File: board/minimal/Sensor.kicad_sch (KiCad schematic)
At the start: 27 parts, among them Q2 DMP6050SSD, U5 TLV73318PDBV, U6 PCA9306D, U7 ICM-20948, U8 BME280, U9 INA260

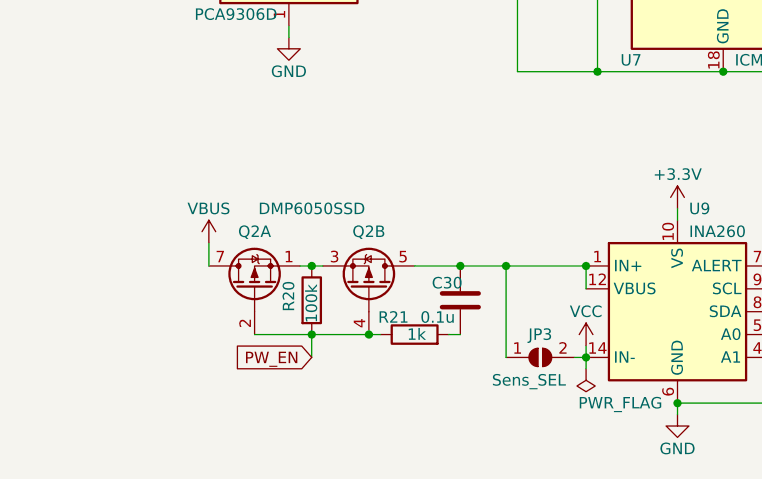
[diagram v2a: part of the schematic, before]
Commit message: add some connectors
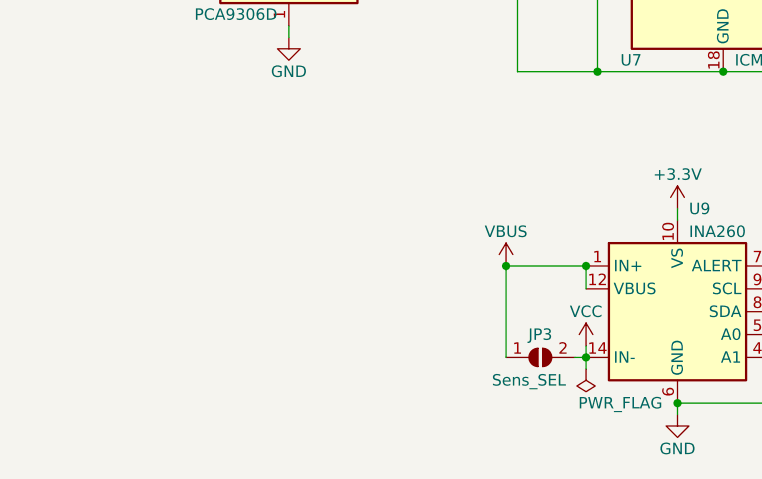
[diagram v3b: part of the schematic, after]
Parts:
- removed C30: 0.1u, Capacitor_SMD:C_0201_0603Metric, symbol Device:C
- removed Q2: DMP6050SSD, Package_SO:SOIC-8_3.9x4.9mm_P1.27mm, symbol Transistor_FET:DMP6050SSD
- removed R20: 100k, Resistor_SMD:R_0603_1608Metric, symbol Device:R
- removed R21: 1k, Resistor_SMD:R_0603_1608Metric, symbol Device:R
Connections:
- net VBUS: now also JP3.1 (A), U9.1 (IN+), U9.12 (VBUS), U9.2 (IN+), U9.3 (IN+)

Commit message: change imu to BNO086
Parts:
- removed C23, C24: 1u, Capacitor_SMD:C_0201_0603Metric, symbol Device:C
- removed C25, C26, C27: 0.1u, Capacitor_SMD:C_0201_0603Metric, symbol Device:C
- removed JP1: I2C_Addr, Jumper:SolderJumper-2_P1.3mm_Open_RoundedPad1.0x1.5mm, symbol Jumper:SolderJumper_2_Open
- removed R13: 10k, Resistor_SMD:R_0603_1608Metric, symbol Device:R
- removed R14, R15, R16, R17: 1k, Resistor_SMD:R_0603_1608Metric, symbol Device:R
- removed R18: 200k, Resistor_SMD:R_0603_1608Metric, symbol Device:R
- removed U5: TLV73318PDBV, Package_TO_SOT_SMD:SOT-23-5, symbol Regulator_Linear:TLV73318PDBV
- removed U6: PCA9306D, Package_SON:X2SON-8_1.4x1mm_P0.35mm, symbol Interface:PCA9306D
- removed U7: ICM-20948, Sensor_Motion:InvenSense_QFN-24_3x3mm_P0.4mm, symbol Sensor_Motion:ICM-20948
- added C12, C21: 20p, Capacitor_SMD:C_0201_0603Metric, symbol Device:C
- added C22: 0.1u, Capacitor_SMD:C_0201_0603Metric, symbol Device:C
- added C45, C46: 100n, Capacitor_SMD:C_0201_0603Metric, symbol Device:C
- added R35, R36: 10k, Resistor_SMD:R_0603_1608Metric, symbol Device:R
- added TP6: BNO_{BOOT}, symbol Connector:TestPoint
- added U3: BNO086, BNO086, symbol BNO086:BNO086
- added Y1: ABS06-32.768KHZ-T, symbol Device:Crystal
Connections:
- net +1V8 is gone; now on net +3.3V: C28.1, C29.1
- net +3.3V: now also C45.1, C46.1, R35.1, R36.1, U3.28 (VDDIO), U3.3 (VDD)
- net GND: now also C12.1, C21.1, C22.1, C45.2, C46.2, U3.10 (CLKSEL0), U3.17 (SA0/H_MOSI), U3.2 (GND_1), U3.25 (GND_2), U3.5 (PS1), U3.6 (PS0/WAKE)
- net SCL: now also U3.19 (H_SCL/SCK/RX)
- net SDA: now also U3.20 (H_SDA/H_MISO/TX)
- new net: C21.2, U3.27 (XIN32), Y1.1
- new net: R36.2, U3.11 (NRST)
- new net: C12.2, U3.26 (XOUT32/CLKSEL1), Y1.2
- new net: R35.2, TP6.1, U3.4 (BOOTN)
- new net: C22.2, U3.9 (CAP)
- no-connect marks 4 -> 14
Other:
- moved on the sheet: C28, C29, C31, JP2, JP3, R19, U8, U9

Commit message: set footprint
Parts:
- TP1: renamed from TP6; footprint (none) -> TestPoint:TestPoint_Loop_D2.50mm_Drill1.85mm
- U7: renamed from U3; footprint BNO086 -> BNO086:BNO086
- Y2: renamed from Y1; footprint (none) -> ABRACON_Crystal:ABS06
- renumbered C45 to C28, C46 to C29, C22 to C30, C28 to C32, C29 to C33, C12 to C34, C21 to C35, JP3 to JP2, JP2 to JP3, R35 to R20, R36 to R21, R19 to R22, U9 to U6
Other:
- moved on the sheet: C31, JP2, U6

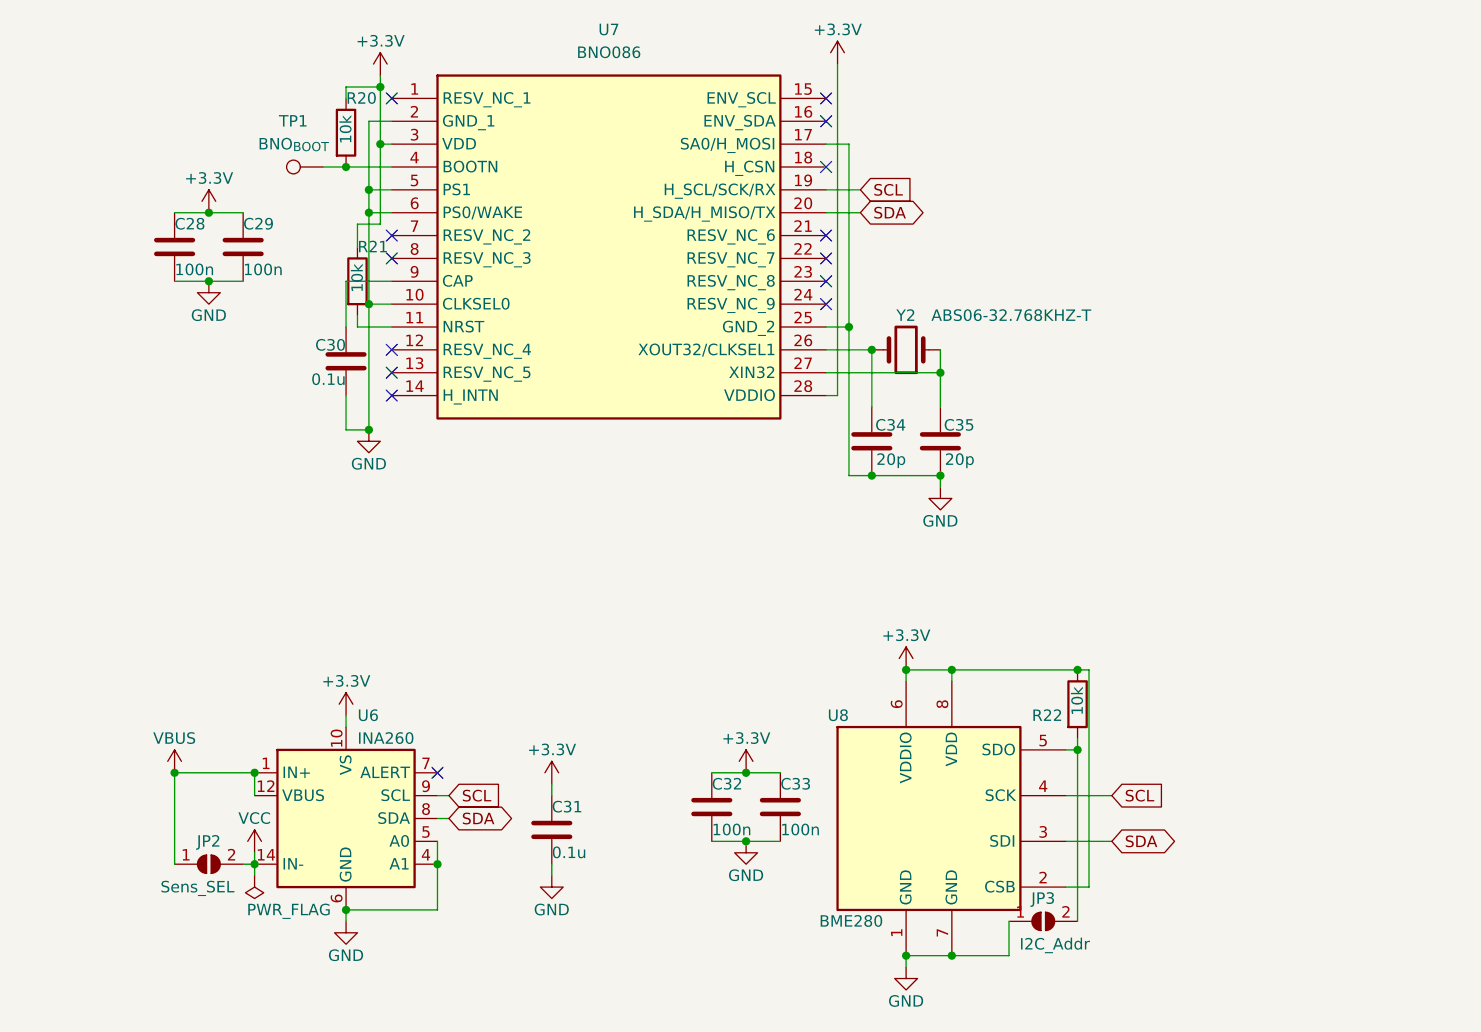
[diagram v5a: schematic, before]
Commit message: add testpoint for gnd and pic of schematics
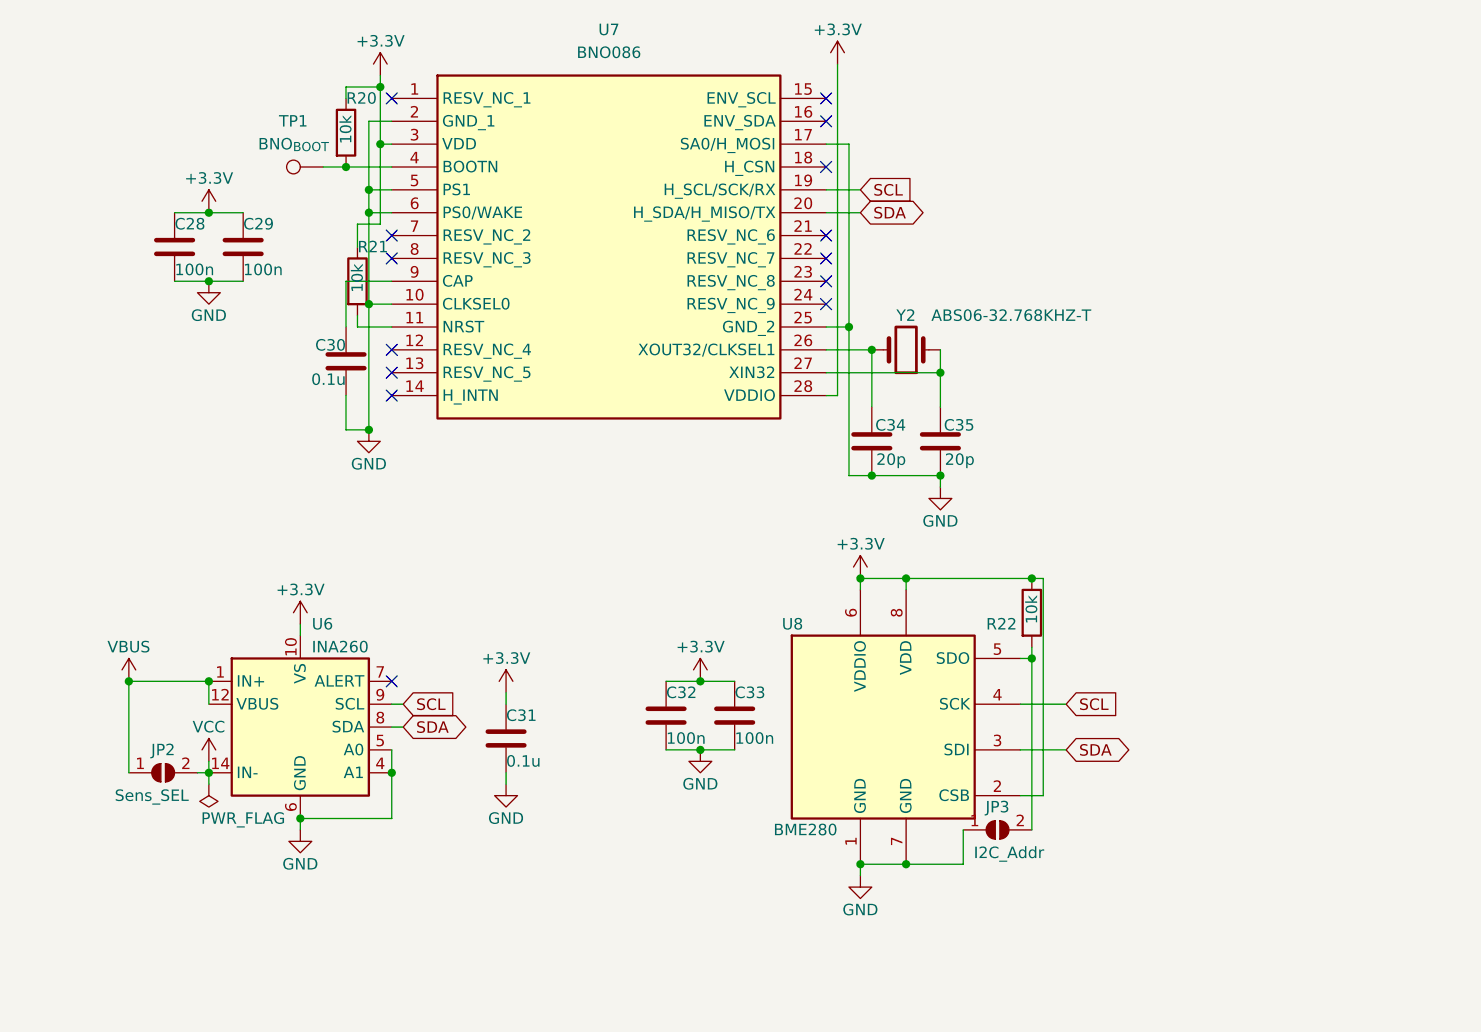
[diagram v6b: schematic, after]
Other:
- moved on the sheet: C31, C32, C33, JP2, JP3, R22, U6, U8
